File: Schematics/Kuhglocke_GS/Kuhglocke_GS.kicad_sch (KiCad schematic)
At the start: 152 parts, among them IC1 P3T1755DPZ, J2 MSD-1-A MicroSD Slot, J4 1S Li-Ion Cell, J4 USB_C_Female_USB2_Small, J5 Speaker, J6 MB_A, J7 MB_B, J8 DB_A, J9 DB_B, Q1 AO3401A, Q2 MMBT3904, Q3 AO3401A, Q4 AO3400A, Q5 MMBT3904, Q6 AO3401A, Q7 AO3400A, SW1 PWR, SW2 SW_BACK, SW2 SW_DOWN, SW2 SW_ENTER, SW2 SW_ESP_BOOT_MODE, SW2 SW_ESP_RESET, SW2 SW_UP, U1 CP2102N-Axx-xQFN28, U1 RFM95W-915S2, U10 TPB4056B2X-ES1R, U12 AMS1117-3.3, U12 NAU7802SGI, U2 ESP32-S3-WROOM-1, U4 LM66100DCKR, U5 LM66100DCKR, U7 MAX98357AETE_T, U8 ACS70331EOLC, U8 TPS63001DRCR, U9 YIC31616GMSGG GPS

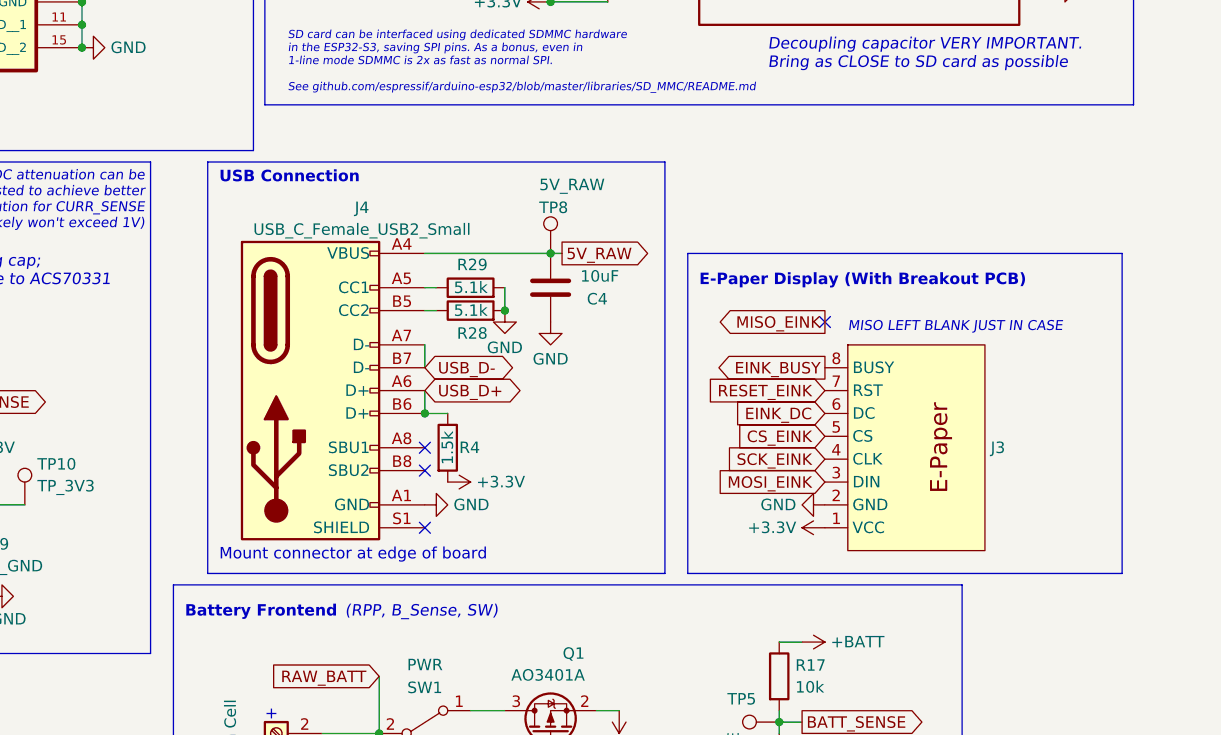
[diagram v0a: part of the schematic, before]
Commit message: init commit for migrating avionics comms devices to dedicated repo  - updated datasheets links to local file  - missing exact LoRaSX162 datasheet
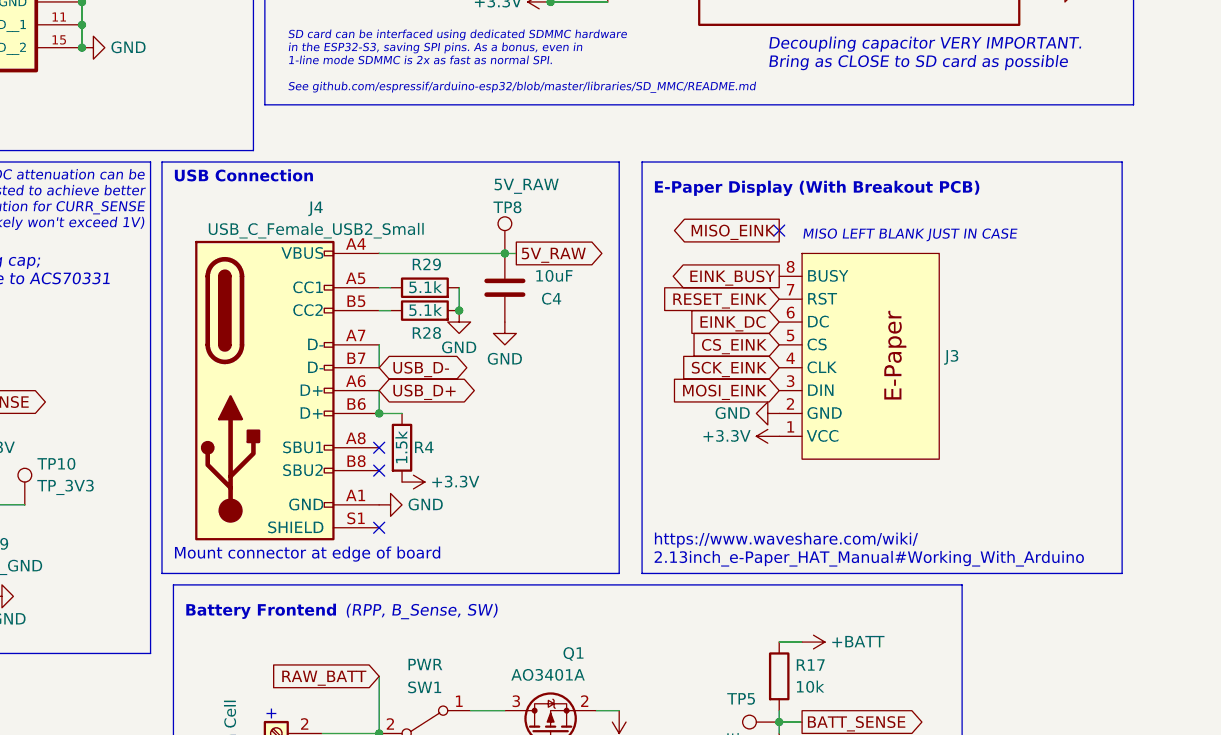
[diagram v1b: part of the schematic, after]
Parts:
- J4: Digikey (none) -> ED10561-ND
- SW1: Digikey (none) -> 108-SS-12D07-VG4NSGAPA-ND
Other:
- note added: "https://www.waveshare.com/wiki/ 2.13inch_e-Paper_HAT_Manual#Working_With_Arduino"
- moved on the sheet: C4, J3, J4, R28, R29, R4, TP8
